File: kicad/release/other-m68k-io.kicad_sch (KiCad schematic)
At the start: 19 parts, among them J11 FTDI B (GND CTS VCC TXD RXD R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, J2 FTDI (GND CTS VCC TXD RXD RTS), SW1 RESET, U10 MC68681P, U13 MCP130T-450I/TT, Y1 3.6864MHz

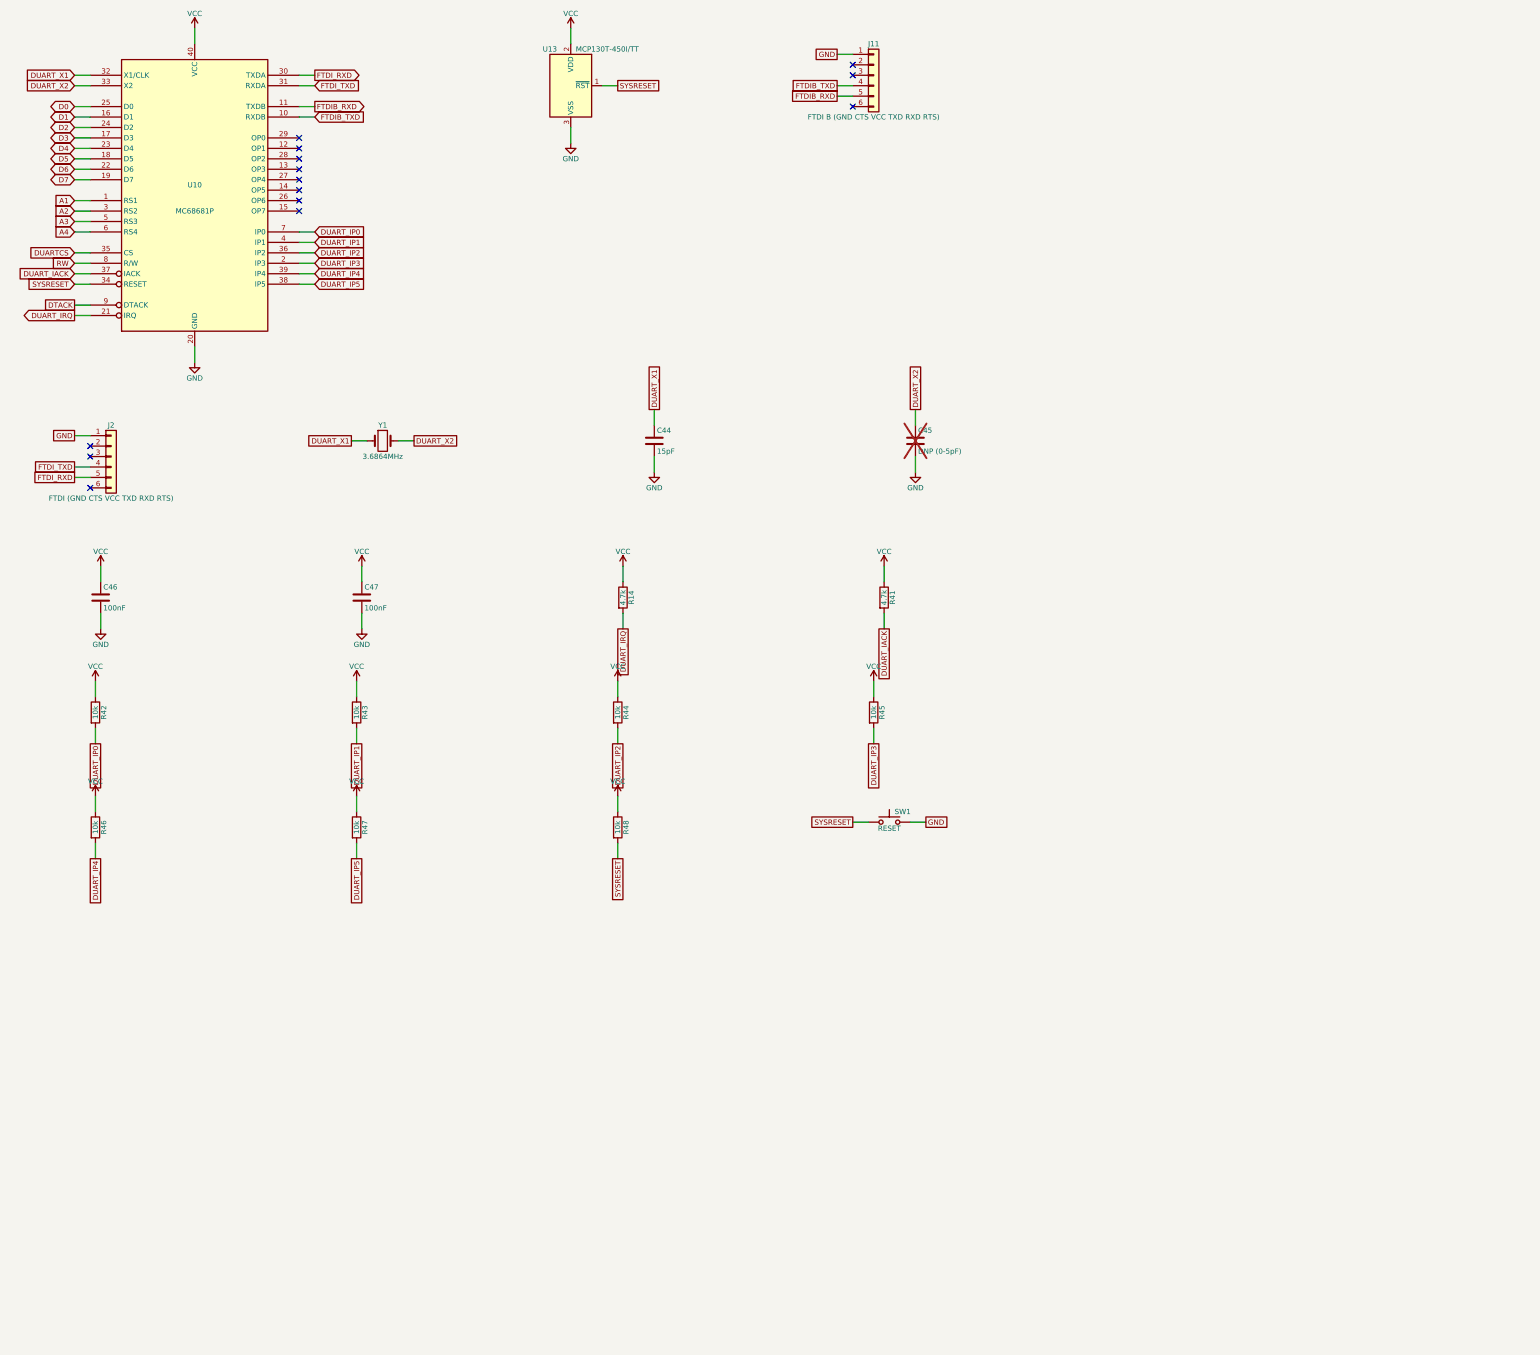
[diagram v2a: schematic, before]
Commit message: spec rev 11 / board rev C3: Atari joystick and paddle port on the DUART's I/O pins
Hardware: J12, a DE-9 male with the Atari pinout on the front edge. The five switches go
through 1 k into DUART inputs IP0..IP4 (up, down, left, right, fire), which already have
10 k pull-ups. Paddles: each pot charges, through 1 k, a 15 nF capacitor; a 74HC14 gate
(U14) pulls the up (A) or down (B) line low through a BAT54W when the capacitor passes its
threshold, so those lines double as end-of-charge signals (a joystick has no pots, paddles
no up/down switches); a dual NPN (Q1) on OP0 shorts both capacitors (pin high = shorted,
the reset state); +5 V through a 200 mA polyfuse. Paddle A's button is on pin 4 (right),
B's on pin 3 (left). The dedication moved under the SRAMs to make room. Routed with the
optimizer off: 0 DRC violations, 0 unrouted; fab package and release regenerated; the six
new part numbers are flagged verify in parts.json.

Firmware (fw/joy.c): sys_joystick (40) returns the JOY_* mask from one input-port read.
sys_paddles (41) fills struct paddles {a, b 0..1023 (1023 = 12 ms = 2764 counts), valid
bits, frame}: the first call starts measuring, NULL or program exit stops it. The
counter/timer runs free in timer mode from X1/16 (230.4 kHz) and IP0/IP1 change
interrupts are enabled (ACR 0x73, IMR.IPC). Each frame the VBLANK handler shorts the
capacitors; when the DUART reports the lines rising (its 38.4 kHz sampler has seen the
step) the level-3 handler releases them and notes the counter, and it timestamps each
fall; if nothing rose the next VBLANK releases directly. Measured in the emulator: 0.2 %
of the CPU with no paddle, 1.8 % with two. A joystick held up/down while measuring reads
as no paddle; a program using the counter/timer itself must not use paddles.

Spec: joystick section, DUART IPCR/ACR/IP/OPR fields, syscalls 40-41, struct paddles,
JOY_*/PADDLE_* constants. Emulator: joy.c models the port (--joy switches, --paddle A,B
or a game controller's triggers, SD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
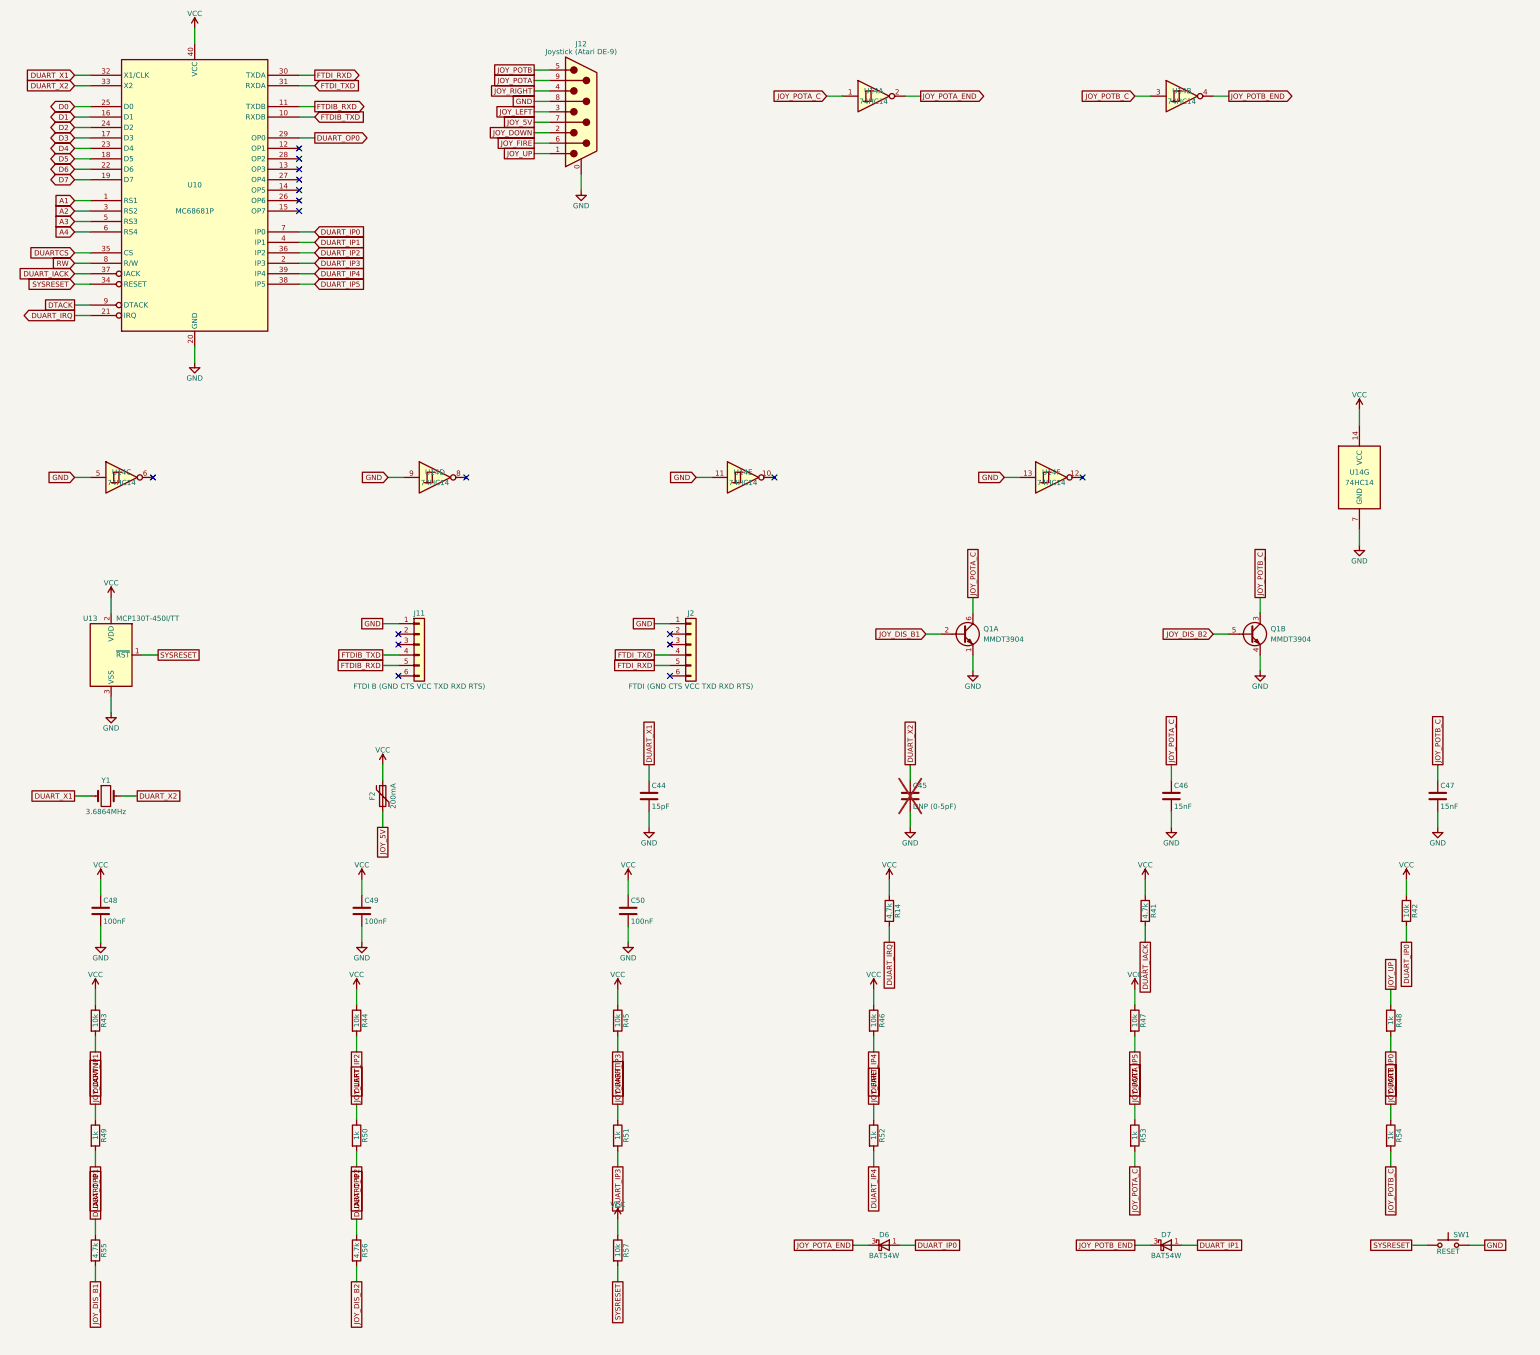
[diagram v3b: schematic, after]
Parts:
- added C48, C49, C50: 100nF, Capacitor_SMD:C_0603_1608Metric, symbol Device:C
- added D6, D7: BAT54W, Package_TO_SOT_SMD:SOT-323_SC-70, symbol Diode:BAT54W
- added F2: 200mA, Fuse:Fuse_1206_3216Metric, symbol Device:Polyfuse
- added J12: Joystick (Atari DE-9), Connector_Dsub:DSUB-9_Pins_Horizontal_P2.77x2.84mm_EdgePinOffset7.70mm_Housed_MountingHolesOffset9.12mm, symbol Connector:DE9_Pins_MountingHoles
- added Q1: MMDT3904, Package_TO_SOT_SMD:SOT-363_SC-70-6, symbol Transistor_BJT:MMDT3904
- added R49, R50, R51, R52, R53, R54: 1k, Resistor_SMD:R_0603_1608Metric, symbol Device:R
- added R55, R56: 4.7k, Resistor_SMD:R_0603_1608Metric, symbol Device:R
- added R57: 10k, Resistor_SMD:R_0603_1608Metric, symbol Device:R
- added U14: 74HC14, Package_SO:SOIC-14_3.9x8.7mm_P1.27mm, symbol 74xx:74HC14
- C46: value 100nF -> 15nF; Desc 100 nF 50 V X7R 0603 -> 15 nF 50 V X7R 0603; LCSC C1591 -> C1710; MPN CL10B104KB8NNNC -> CL10B153KB8NNNC; PcbNear U10 -> U14
- C47: value 100nF -> 15nF; Desc 100 nF 50 V X7R 0603 -> 15 nF 50 V X7R 0603; LCSC C1591 -> C1710; MPN CL10B104KB8NNNC -> CL10B153KB8NNNC; PcbNear U13 -> U14
- R48: value 10k -> 1k; Desc 10 k 1% 0603 -> 1 k 1% 0603; LCSC C25804 -> C21190; MPN RC0603FR-0710KL -> RC0603FR-071KL; PcbNear U13 -> J12
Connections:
- net DUART_IP0: now also R48.2, D6.1 (A)
- net DUART_IP1: now also D7.1 (A), R49.2
- net DUART_IP2: now also R50.2
- net DUART_IP3: now also R51.2
- net DUART_IP4: now also R52.2
- net GND: now also C48.2, C49.2, C50.2, J12.0 (PAD), J12.8, Q1.1 (E1), Q1.4 (E2), U14.11, U14.13, U14.5, U14.7 (GND), U14.9
- net SYSRESET: now also R57.2; no longer R48.2
- net VCC: now also C48.1, C49.1, C50.1, F2.1, R57.1, U14.14 (VCC); no longer C46.1, C47.1, R48.1
- net DUART_OP0: now reaches U10.29 (OP0)
- net DUART_OP0: now also R55.1, R56.1
- new net JOY_5V: F2.2, J12.7
- new net JOY_DIS_B1: Q1.2 (B1), R55.2
- new net JOY_DIS_B2: Q1.5 (B2), R56.2
- new net JOY_DOWN: J12.2, R49.1
- new net JOY_FIRE: J12.6, R52.1
- new net JOY_LEFT: J12.3, R50.1
- new net JOY_POTA: J12.9, R53.1
- new net JOY_POTA_C: C46.1, Q1.6 (C1), R53.2, U14.1
- new net JOY_POTA_END: D6.3 (K), U14.2
- new net JOY_POTB: J12.5, R54.1
- new net JOY_POTB_C: C47.1, Q1.3 (C2), R54.2, U14.3
- new net JOY_POTB_END: D7.3 (K), U14.4
- new net JOY_RIGHT: J12.4, R51.1
- new net JOY_UP: J12.1, R48.1
- no-connect marks 14 -> 17
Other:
- moved on the sheet: C44, C45, C46, C47, J11, J2, R14, R41, R42, R43, R44, R45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

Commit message: rev C3 release: BOM regenerated with the verified part descriptions
Co-Authored-By: Claude Fable 5.1 <noreply@anthropic.com>
Claude-Session: https://claude.ai/code/session_019bbFLKMxhKXGW6aABP44Z1
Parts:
- C46, C47: Desc 15 nF 50 V X7R 0603 -> 15 nF 50 V X7R 0603 (Avnet/Future stock; any 0603 X7R 15 nF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; LCSC C1710 -> (none)
- D6, D7: Desc Schottky diode 30 V 200 mA, SOT-323 -> Schottky diode 30 V 200 mA, SOT-323 (DigiKey/Mouser/LCSC st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; LCSC C2290615 -> C8657
- F2: Desc PTC resettable fuse 0.2 A hold / 0.4 A trip, 1206 -> PTC resettable fuse 0.2 A hold / 0.42 A trip, 24 V, 1206 (D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
- J12: Desc DE-9 male, right angle, housed, 4-40 boardlocks (Atari joys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 -> DE-9 male (plug), right angle, housed, 4-40 boardlocks, .31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
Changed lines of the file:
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@@
 			)
 		)
-		(property "LCSC" "C2290615"
+		(property "LCSC" "C8657"
 			(at 306.07 317.5 0)
 			(effects
@@
 			)
 		)
-		(property "Desc" "Schottky diode 30 V 200 mA, SOT-323"
+		(property "Desc" "Schottky diode 30 V 200 mA, SOT-323 (DigiKey/Mouser/LCSC stocked)"
 			(at 306.07 317.5 0)
 			(effects
@@
 			)
 		)
-		(property "LCSC" "C1710"
-			(at 372.11 208.28 0)
-			(effects
-				(font
-					(size 1.27 1.27)
-				)
-				(hide yes)
-			)
-		)
-		(property "Desc" "15 nF 50 V X7R 0603"
+		(property "Desc" "15 nF 50 V X7R 0603 (Avnet/Future stock; any 0603 X7R 15 nF 50 V is fine)"
 			(at 372.11 208.28 0)
 			(effects
@@
 			)
 		)
-		(property "LCSC" "C2290615"
+		(property "LCSC" "C8657"
 			(at 237.49 317.5 0)
 			(effects
@@
 			)
 		)
-		(property "Desc" "Schottky diode 30 V 200 mA, SOT-323"
+		(property "Desc" "Schottky diode 30 V 200 mA, SOT-323 (DigiKey/Mouser/LCSC stocked)"
 			(at 237.49 317.5 0)
 			(effects
@@
 			)
 		)
-		(property "LCSC" "C1710"
-			(at 307.34 208.28 0)
-			(effects
-				(font
-					(size 1.27 1.27)
-				)
-				(hide yes)
-			)
-		)
-		(property "Desc" "15 nF 50 V X7R 0603"
+		(property "Desc" "15 nF 50 V X7R 0603 (Avnet/Future stock; any 0603 X7R 15 nF 50 V is fine)"
 			(at 307.34 208.28 0)
 			(effects
@@
 			)
 		)
-		(property "Desc" "PTC resettable fuse 0.2 A hold / 0.4 A trip, 1206"
+		(property "Desc" "PTC resettable fuse 0.2 A hold / 0.42 A trip, 24 V, 1206 (DigiKey/Element14)"
 			(at 115.57 208.28 0)
 			(effects
@@
 			)
 		)
-		(property "Desc" "DE-9 male, right angle, housed, 4-40 boardlocks (Atari joystick port)"
+		(property "Desc" "DE-9 male (plug), right angle, housed, 4-40 boardlocks, .318 in (8.08 mm) backset = KiCad's EdgePinOffset7.70/MountingHolesOffset9.12 footprint; DigiKey stocks it as L717SDE09PA4CH4FA610, Farnell as L717SDE09PA4CH4F (any L717SDE09PA4CH4x is the same connector)"
 			(at 163.83 41.91 0)
 			(effects
